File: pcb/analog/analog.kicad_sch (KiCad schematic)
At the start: 65 parts, among them J1 USB_C_Receptacle_USB2.0, SW1 SW_Push, SW2 SW_Push, U1 SRV05-4, U2 XC6206P332MR, U3 DRV5056A3xDBZxQ1, U4 DRV5056A3xDBZxQ1, U5 DRV5056A3xDBZxQ1, U6 74AHCT1G125, U7 74AHCT1G125, U8 RP2040, U9 W25Q128JVS, Y1 12MHz

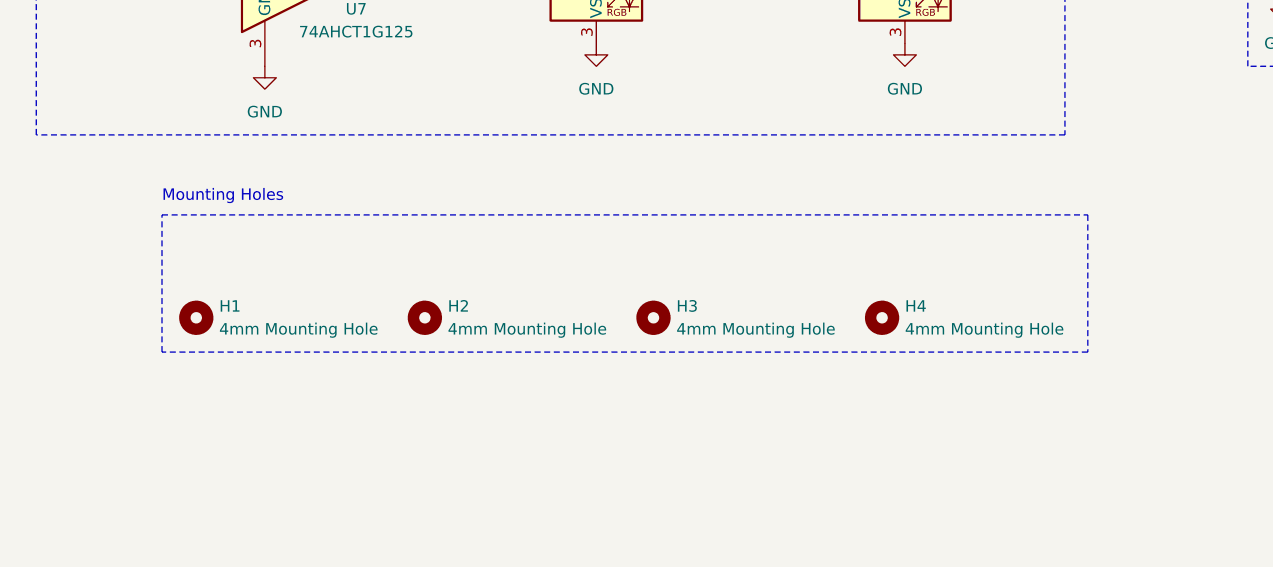
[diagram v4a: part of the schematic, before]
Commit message: chore: rename mounting holes in schematic
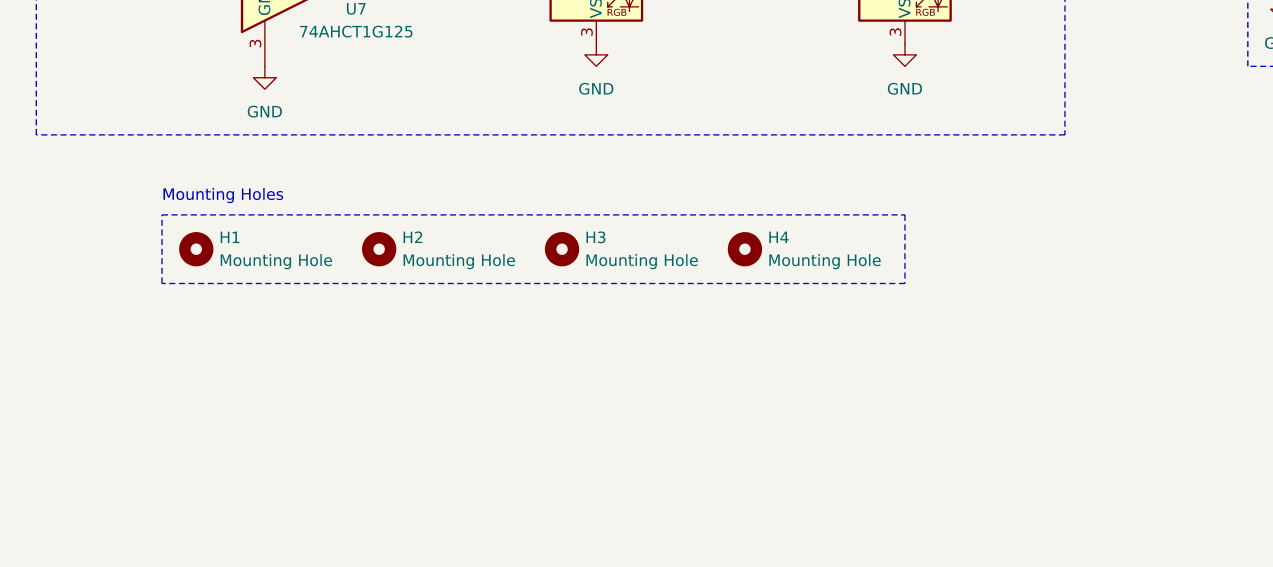
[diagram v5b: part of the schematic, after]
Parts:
- H1, H2, H3, H4: value 4mm Mounting Hole -> Mounting Hole
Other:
- moved on the sheet: H1, H2, H3, H4
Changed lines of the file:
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@@
     (fill (type none))
   )
-  (rectangle (start 173.99 168.91) (end 276.86 184.15)
+  (rectangle (start 173.99 168.91) (end 256.54 176.53)
     (stroke (width 0) (type dash))
     (fill (type none))
@@
     )
   )
-  (symbol (lib_id "Mechanical:MountingHole") (at 203.2 180.34 0) (unit 1)
+  (symbol (lib_id "Mechanical:MountingHole") (at 198.12 172.72 0) (unit 1)
     (in_bom yes) (on_board yes) (dnp no) (fields_autoplaced)
-    (property "Reference" "H2" (at 205.74 179.07 0)
+    (property "Reference" "H2" (at 200.66 171.45 0)
       (effects (font (size 1.27 1.27)) (justify left))
     )
-    (property "Value" "4mm Mounting Hole" (at 205.74 181.61 0)
+    (property "Value" "Mounting Hole" (at 200.66 173.99 0)
       (effects (font (size 1.27 1.27)) (justify left))
     )
-    (property "Footprint" "MountingHole:MountingHole_4mm" (at 203.2 180.34 0)
+    (property "Footprint" "MountingHole:MountingHole_4mm" (at 198.12 172.72 0)
       (effects (font (size 1.27 1.27)) hide)
     )
-    (property "Datasheet" "~" (at 203.2 180.34 0)
+    (property "Datasheet" "~" (at 198.12 172.72 0)
       (effects (font (size 1.27 1.27)) hide)
     )
@@
     )
   )
-  (symbol (lib_id "Mechanical:MountingHole") (at 228.6 180.34 0) (unit 1)
+  (symbol (lib_id "Mechanical:MountingHole") (at 218.44 172.72 0) (unit 1)
     (in_bom yes) (on_board yes) (dnp no) (fields_autoplaced)
-    (property "Reference" "H3" (at 231.14 179.07 0)
+    (property "Reference" "H3" (at 220.98 171.45 0)
       (effects (font (size 1.27 1.27)) (justify left))
     )
-    (property "Value" "4mm Mounting Hole" (at 231.14 181.61 0)
+    (property "Value" "Mounting Hole" (at 220.98 173.99 0)
       (effects (font (size 1.27 1.27)) (justify left))
     )
-    (property "Footprint" "MountingHole:MountingHole_4mm" (at 228.6 180.34 0)
+    (property "Footprint" "MountingHole:MountingHole_4mm" (at 218.44 172.72 0)
       (effects (font (size 1.27 1.27)) hide)
     )
-    (property "Datasheet" "~" (at 228.6 180.34 0)
+    (property "Datasheet" "~" (at 218.44 172.72 0)
       (effects (font (size 1.27 1.27)) hide)
     )
@@
     )
   )
-  (symbol (lib_id "Mechanical:MountingHole") (at 177.8 180.34 0) (unit 1)
+  (symbol (lib_id "Mechanical:MountingHole") (at 177.8 172.72 0) (unit 1)
     (in_bom yes) (on_board yes) (dnp no)
-    (property "Reference" "H1" (at 180.34 179.07 0)
+    (property "Reference" "H1" (at 180.34 171.45 0)
       (effects (font (size 1.27 1.27)) (justify left))
     )
-    (property "Value" "4mm Mounting Hole" (at 180.34 181.61 0)
+    (property "Value" "Mounting Hole" (at 180.34 173.99 0)
       (effects (font (size 1.27 1.27)) (justify left))
     )
-    (property "Footprint" "MountingHole:MountingHole_4mm" (at 177.8 180.34 0)
+    (property "Footprint" "MountingHole:MountingHole_4mm" (at 177.8 172.72 0)
       (effects (font (size 1.27 1.27)) hide)
     )
-    (property "Datasheet" "~" (at 177.8 180.34 0)
+    (property "Datasheet" "~" (at 177.8 172.72 0)
       (effects (font (size 1.27 1.27)) hide)
     )
@@
     )
   )
-  (symbol (lib_id "Mechanical:MountingHole") (at 254 180.34 0) (unit 1)
+  (symbol (lib_id "Mechanical:MountingHole") (at 238.76 172.72 0) (unit 1)
     (in_bom yes) (on_board yes) (dnp no) (fields_autoplaced)
-    (property "Reference" "H4" (at 256.54 179.07 0)
+    (property "Reference" "H4" (at 241.3 171.45 0)
       (effects (font (size 1.27 1.27)) (justify left))
     )
-    (property "Value" "4mm Mounting Hole" (at 256.54 181.61 0)
+    (property "Value" "Mounting Hole" (at 241.3 173.99 0)
       (effects (font (size 1.27 1.27)) (justify left))
     )
-    (property "Footprint" "MountingHole:MountingHole_4mm" (at 254 180.34 0)
+    (property "Footprint" "MountingHole:MountingHole_4mm" (at 238.76 172.72 0)
       (effects (font (size 1.27 1.27)) hide)
     )
-    (property "Datasheet" "~" (at 254 180.34 0)
+    (property "Datasheet" "~" (at 238.76 172.72 0)
       (effects (font (size 1.27 1.27)) hide)
     )

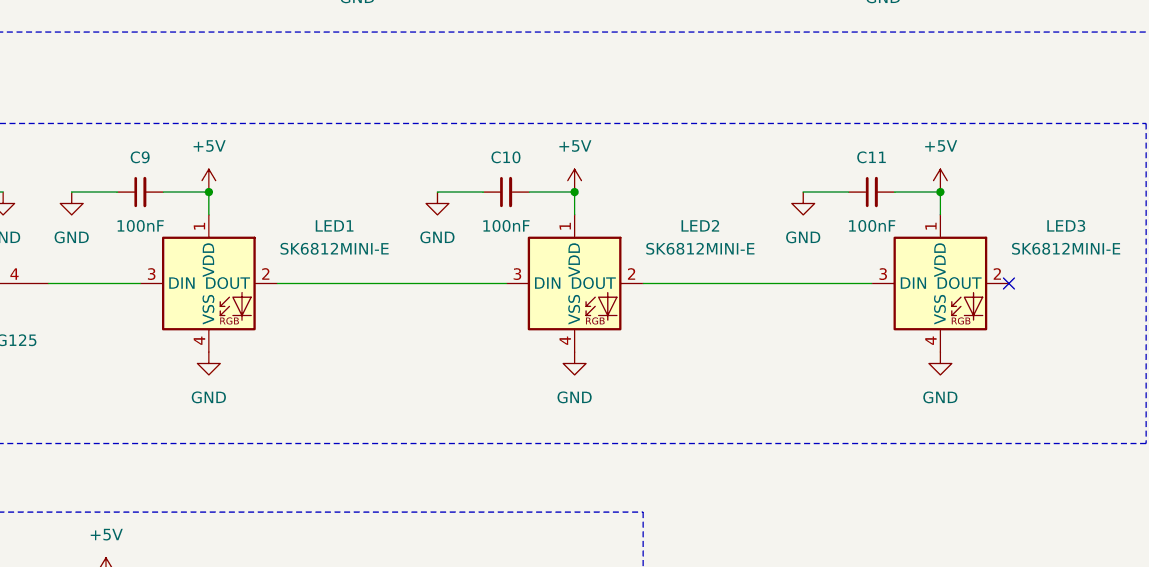
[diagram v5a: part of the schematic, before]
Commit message: fix: resolve footprint mismatch warnings
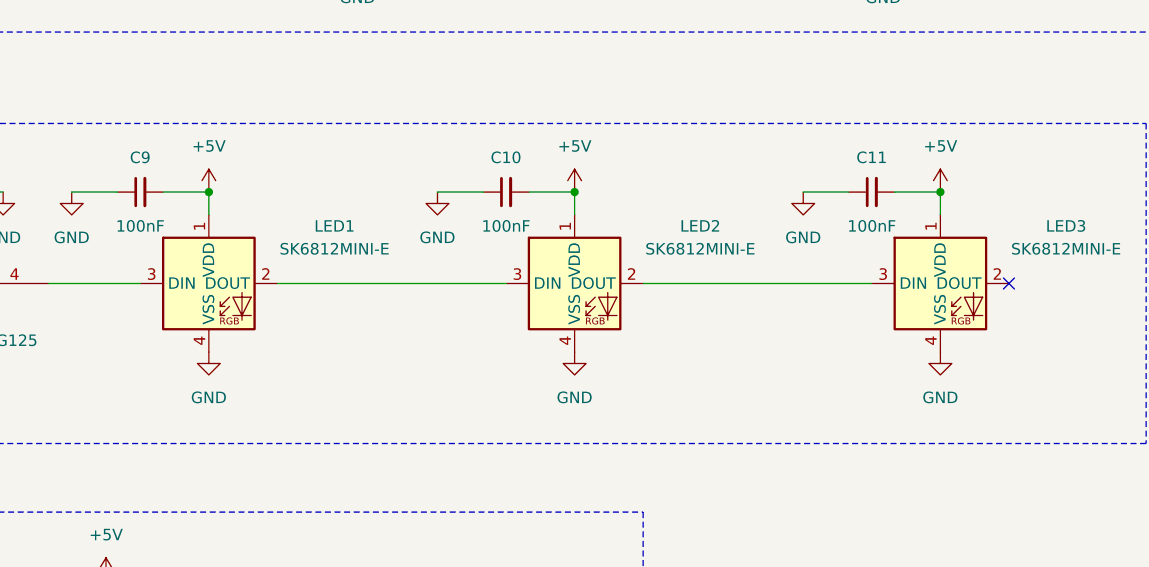
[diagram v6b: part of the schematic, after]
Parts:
- LED1, LED2, LED3: symbol PCM_marbastlib-various:SK6812MINI-E -> PCM_marbastlib-mx:MX_SK6812MINI-E
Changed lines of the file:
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@@
     )
   )
-  (symbol (lib_id "PCM_marbastlib-various:SK6812MINI-E") (at 226.06 91.44 0) (unit 1)
+  (symbol (lib_id "PCM_marbastlib-mx:MX_SK6812MINI-E") (at 226.06 91.44 0) (unit 1)
     (in_bom yes) (on_board yes) (dnp no)
     (property "Reference" "LED1" (at 240.03 85.09 0)
@@
     )
   )
-  (symbol (lib_id "PCM_marbastlib-various:SK6812MINI-E") (at 307.34 91.44 0) (unit 1)
+  (symbol (lib_id "PCM_marbastlib-mx:MX_SK6812MINI-E") (at 307.34 91.44 0) (unit 1)
     (in_bom yes) (on_board yes) (dnp no)
     (property "Reference" "LED3" (at 321.31 85.09 0)
@@
     )
   )
-  (symbol (lib_id "PCM_marbastlib-various:SK6812MINI-E") (at 266.7 91.44 0) (unit 1)
+  (symbol (lib_id "PCM_marbastlib-mx:MX_SK6812MINI-E") (at 266.7 91.44 0) (unit 1)
     (in_bom yes) (on_board yes) (dnp no)
     (property "Reference" "LED2" (at 280.67 85.09 0)

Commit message: refactor: use 1206 footprint for fuse
there are more polyfuses with 500mA hold current at this size.
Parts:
- F1: footprint Fuse:Fuse_0805_2012Metric -> Fuse:Fuse_1206_3216Metric
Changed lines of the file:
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@@
       (effects (font (size 1.27 1.27)))
     )
-    (property "Footprint" "Fuse:Fuse_0805_2012Metric" (at 49.53 29.21 0)
+    (property "Footprint" "Fuse:Fuse_1206_3216Metric" (at 49.53 29.21 0)
       (effects (font (size 1.27 1.27)) (justify left) hide)
     )

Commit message: feat: setup bom and initial gerbers files
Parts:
- C1, C12, C16, C2, C28, C3, C4, C5, C6, C7, C8: LCSC (none) -> C52923
- C10, C11, C13, C14, C17, C18, C19, C20, C21, C22, C23, C26, C27, C9: LCSC (none) -> C1525
- C15: LCSC (none) -> C19702
- C24, C25: LCSC (none) -> C1555
- D1, D2: LCSC (none) -> C2761795
- F1: LCSC (none) -> C170165
- J1: LCSC (none) -> C165948
- LED1, LED2, LED3: LCSC (none) -> C5149201
- R1, R10, R12, R13, R2: LCSC (none) -> C25905
- R11, R9: LCSC (none) -> C25100
- R14, R6, R7, R8: LCSC (none) -> C11702
- R3, R4, R5: LCSC (none) -> C25076
- SW1, SW2: LCSC (none) -> C318884
- U1: LCSC (none) -> C2836319
- U2: LCSC (none) -> C5446
- U3, U4, U5: LCSC (none) -> C2152965
- U6, U7: LCSC (none) -> C151417
- U8: LCSC (none) -> C2040
- U9: value W25Q128JVS -> W25Q16JVSSIQ; LCSC (none) -> C131025
- Y1: LCSC (none) -> C9002
